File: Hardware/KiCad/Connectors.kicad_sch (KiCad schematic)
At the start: 55 parts

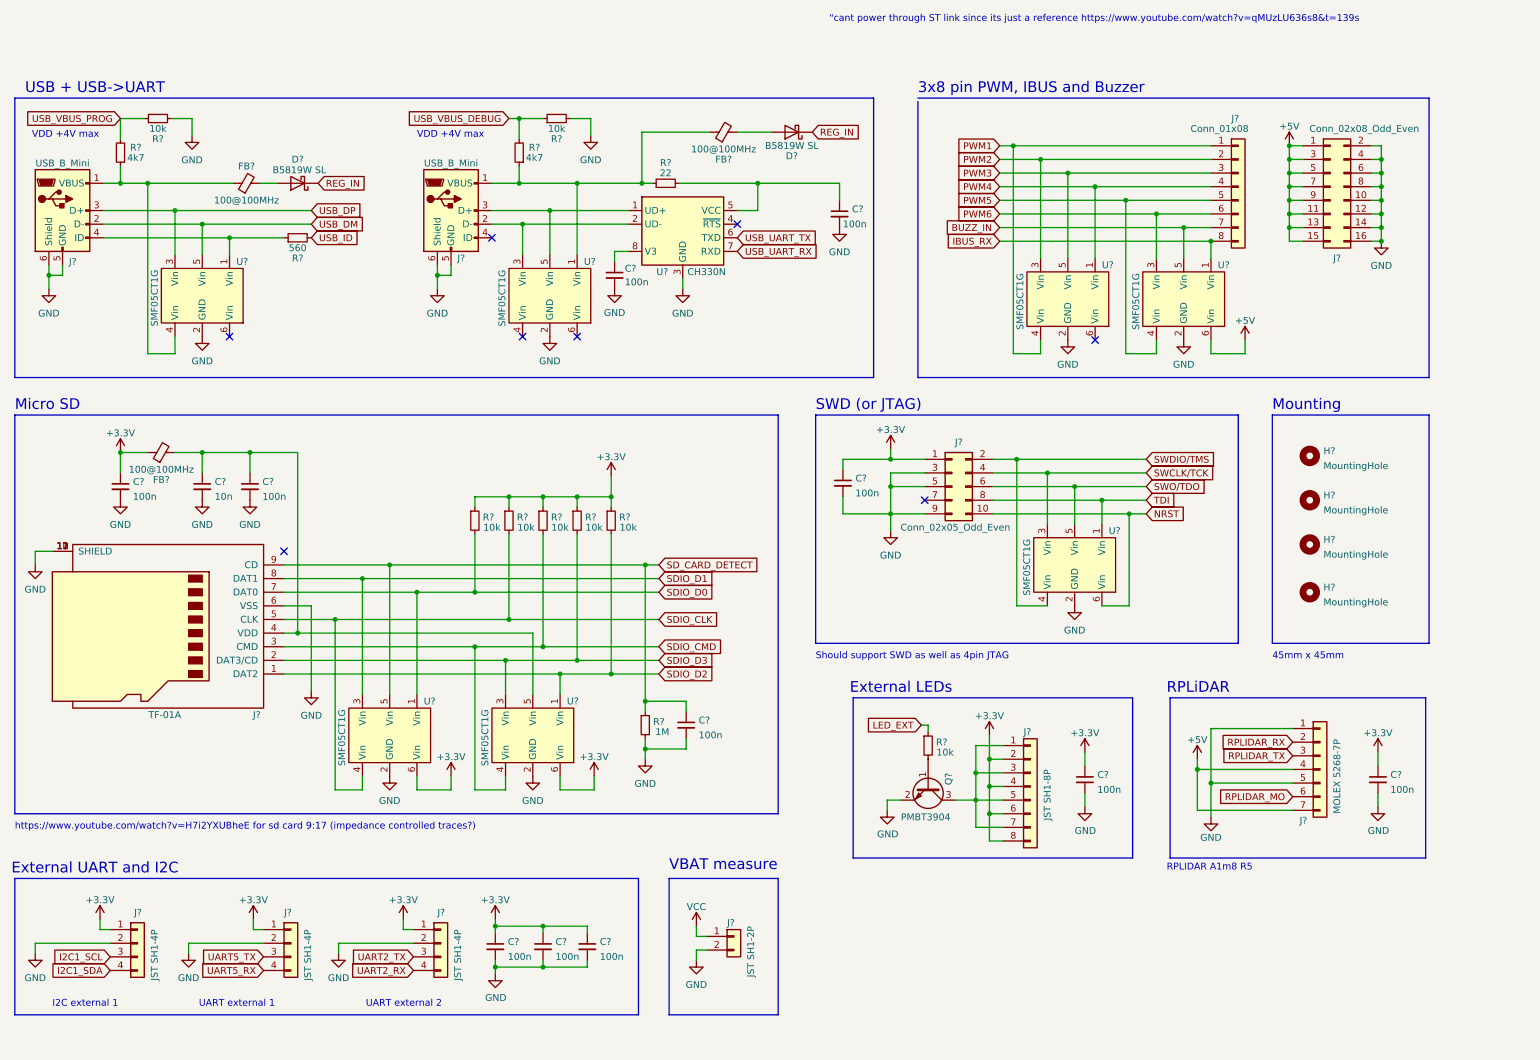
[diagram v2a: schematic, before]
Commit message: Fixed pullup connected to SDIO CLK
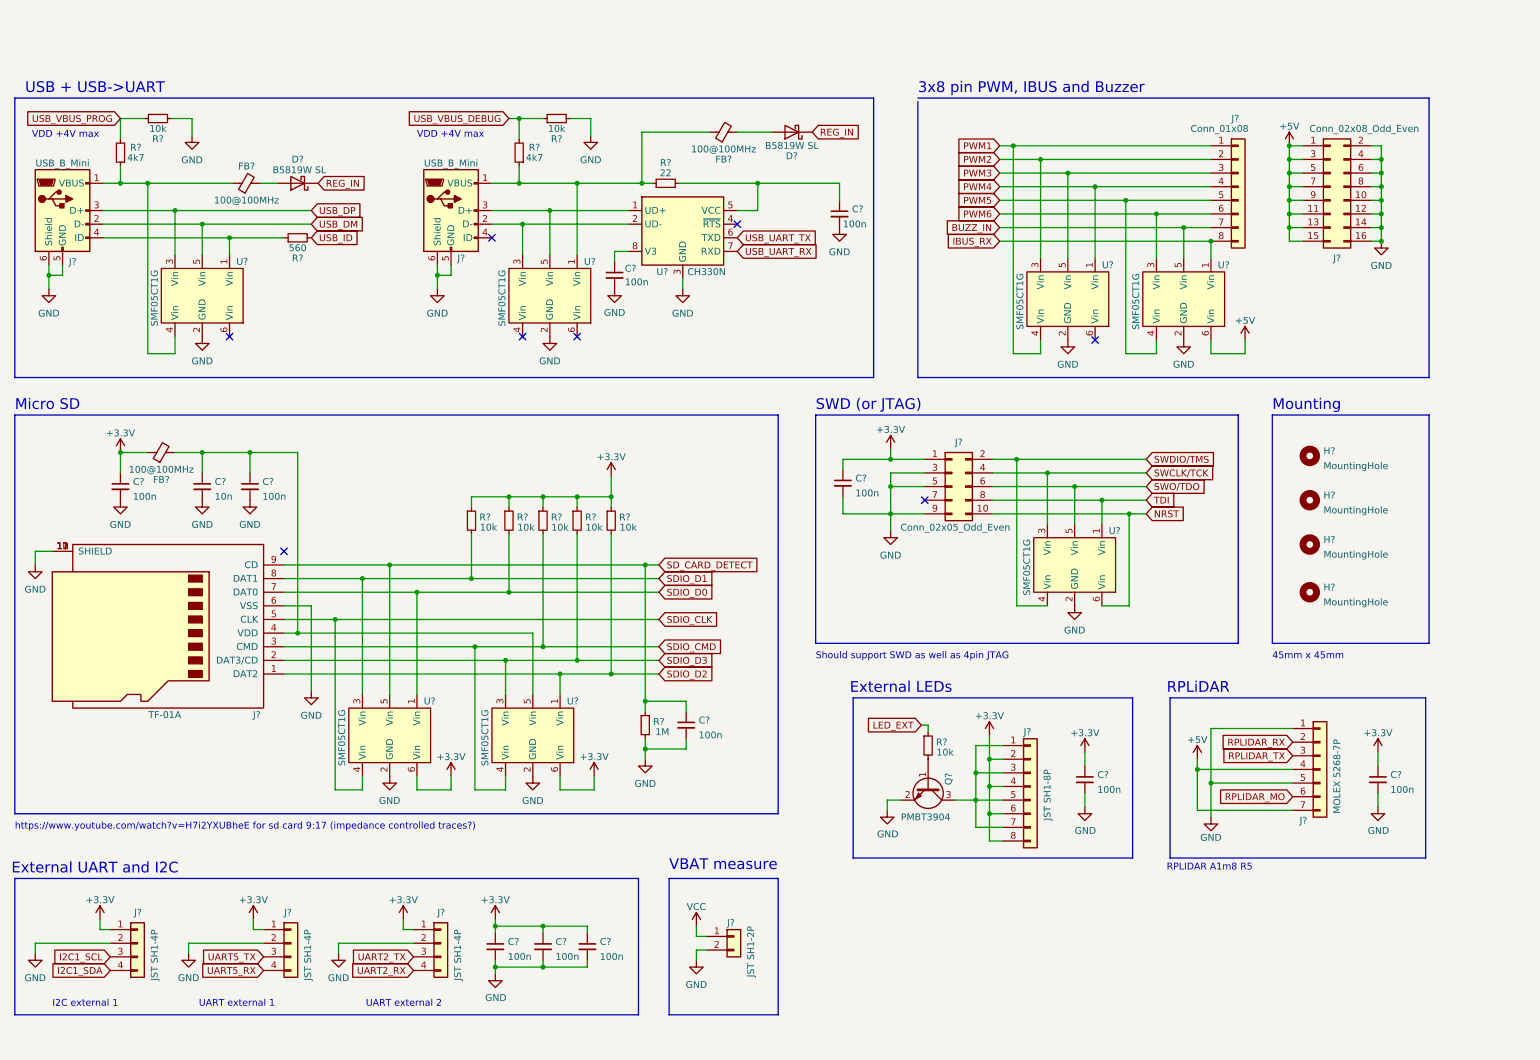
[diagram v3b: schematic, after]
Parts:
- removed R?: 10k, Resistor_SMD:R_0402_1005Metric, symbol Device:R_Small
- added R?: 10k, Resistor_SMD:R_0402_1005Metric, symbol Device:R_Small
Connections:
- net +3V3: now also R?.1
- net SDIO_D1: now also R?.2
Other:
- note removed: ""cant power through ST link since its just a reference https://www.youtube.com/watch?v=qMUzLU636s8&t=139s"
- moved on the sheet: R?
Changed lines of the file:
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@@
   (junction (at 232.41 43.18) (diameter 0) (color 0 0 0 0)
   )
+  (junction (at 116.205 126.365) (diameter 0) (color 0 0 0 0)
+  )
+  (junction (at 252.095 38.1) (diameter 0) (color 0 0 0 0)
+  )
+  (junction (at 196.215 147.32) (diameter 0) (color 0 0 0 0)
+  )
+  (junction (at 125.73 93.345) (diameter 0) (color 0 0 0 0)
+  )
+  (junction (at 227.33 40.64) (diameter 0) (color 0 0 0 0)
+  )
+  (junction (at 54.61 45.085) (diameter 0) (color 0 0 0 0)
+  )
   (junction (at 106.68 93.345) (diameter 0) (color 0 0 0 0)
   )
-  (junction (at 116.205 126.365) (diameter 0) (color 0 0 0 0)
-  )
-  (junction (at 252.095 38.1) (diameter 0) (color 0 0 0 0)
-  )
-  (junction (at 196.215 147.32) (diameter 0) (color 0 0 0 0)
-  )
-  (junction (at 125.73 93.345) (diameter 0) (color 0 0 0 0)
-  )
-  (junction (at 227.33 40.64) (diameter 0) (color 0 0 0 0)
-  )
-  (junction (at 54.61 45.085) (diameter 0) (color 0 0 0 0)
-  )
   (junction (at 108.585 34.925) (diameter 0) (color 0 0 0 0)
   )
@@
   (junction (at 217.17 93.98) (diameter 0) (color 0 0 0 0)
   )
-  (junction (at 106.68 116.205) (diameter 0) (color 0 0 0 0)
-  )
   (junction (at 196.215 142.24) (diameter 0) (color 0 0 0 0)
   )
@@
   (junction (at 269.24 33.02) (diameter 0) (color 0 0 0 0)
   )
+  (junction (at 106.68 111.125) (diameter 0) (color 0 0 0 0)
+  )
   (junction (at 132.08 106.045) (diameter 0) (color 0 0 0 0)
   )
+  (junction (at 99.695 108.585) (diameter 0) (color 0 0 0 0)
+  )
   (junction (at 34.29 34.925) (diameter 0) (color 0 0 0 0)
   )
@@
   )
   (junction (at 269.24 40.64) (diameter 0) (color 0 0 0 0)
-  )
-  (junction (at 100.33 111.125) (diameter 0) (color 0 0 0 0)
   )
   (junction (at 20.955 52.07) (diameter 0) (color 0 0 0 0)
@@
     (stroke (width 0) (type default) (color 0 0 0 0))
   )
-  (wire (pts (xy 74.295 116.205) (xy 106.68 116.205))
+  (wire (pts (xy 74.295 116.205) (xy 134.62 116.205))
     (stroke (width 0) (type default) (color 0 0 0 0))
   )
@@
     (stroke (width 0) (type default) (color 0 0 0 0))
   )
-  (wire (pts (xy 106.68 93.345) (xy 106.68 95.25))
-    (stroke (width 0) (type default) (color 0 0 0 0))
-  )
   (wire (pts (xy 131.445 25.4) (xy 131.445 34.925))
     (stroke (width 0) (type default) (color 0 0 0 0))
@@
     (stroke (width 0) (type default) (color 0 0 0 0))
   )
-  (wire (pts (xy 100.33 95.25) (xy 100.33 93.345))
+  (wire (pts (xy 106.68 95.25) (xy 106.68 93.345))
     (stroke (width 0) (type default) (color 0 0 0 0))
   )
@@
     (stroke (width 0) (type default) (color 0 0 0 0))
   )
+  (wire (pts (xy 106.68 93.345) (xy 113.03 93.345))
+    (stroke (width 0) (type default) (color 0 0 0 0))
+  )
   (wire (pts (xy 64.77 113.665) (xy 69.85 113.665))
     (stroke (width 0) (type default) (color 0 0 0 0))
@@
     (stroke (width 0) (type default) (color 0 0 0 0))
   )
-  (wire (pts (xy 79.375 108.585) (xy 134.62 108.585))
+  (wire (pts (xy 79.375 108.585) (xy 99.695 108.585))
     (stroke (width 0) (type default) (color 0 0 0 0))
   )
@@
     (stroke (width 0) (type default) (color 0 0 0 0))
   )
-  (wire (pts (xy 100.33 111.125) (xy 134.62 111.125))
-    (stroke (width 0) (type default) (color 0 0 0 0))
-  )
   (wire (pts (xy 31.115 40.005) (xy 44.45 40.005))
     (stroke (width 0) (type default) (color 0 0 0 0))
@@
     (stroke (width 0) (type default) (color 0 0 0 0))
   )
-  (wire (pts (xy 100.33 93.345) (xy 106.68 93.345))
+  (wire (pts (xy 99.695 93.345) (xy 106.68 93.345))
     (stroke (width 0) (type default) (color 0 0 0 0))
   )
@@
     (stroke (width 0) (type default) (color 0 0 0 0))
   )
+  (wire (pts (xy 99.695 95.25) (xy 99.695 93.345))
+    (stroke (width 0) (type default) (color 0 0 0 0))
+  )
   (wire (pts (xy 269.24 35.56) (xy 269.24 33.02))
     (stroke (width 0) (type default) (color 0 0 0 0))
@@
     (stroke (width 0) (type default) (color 0 0 0 0))
   )
-  (wire (pts (xy 89.535 111.125) (xy 100.33 111.125))
-    (stroke (width 0) (type default) (color 0 0 0 0))
-  )
   (wire (pts (xy 113.03 179.705) (xy 113.03 180.975))
     (stroke (width 0) (type default) (color 0 0 0 0))
@@
     (stroke (width 0) (type default) (color 0 0 0 0))
   )
-  (wire (pts (xy 106.68 116.205) (xy 134.62 116.205))
-    (stroke (width 0) (type default) (color 0 0 0 0))
-  )
   (wire (pts (xy 121.92 22.86) (xy 121.92 26.035))
     (stroke (width 0) (type default) (color 0 0 0 0))
@@
     (stroke (width 0) (type default) (color 0 0 0 0))
   )
-  (wire (pts (xy 100.33 100.33) (xy 100.33 111.125))
+  (wire (pts (xy 106.68 100.33) (xy 106.68 111.125))
     (stroke (width 0) (type default) (color 0 0 0 0))
   )
@@
     (stroke (width 0) (type default) (color 0 0 0 0))
   )
+  (wire (pts (xy 89.535 111.125) (xy 106.68 111.125))
+    (stroke (width 0) (type default) (color 0 0 0 0))
+  )
   (wire (pts (xy 64.77 108.585) (xy 79.375 108.585))
     (stroke (width 0) (type default) (color 0 0 0 0))
@@
     (stroke (width 0) (type default) (color 0 0 0 0))
   )
+  (wire (pts (xy 106.68 111.125) (xy 134.62 111.125))
+    (stroke (width 0) (type default) (color 0 0 0 0))
+  )
   (wire (pts (xy 74.93 176.53) (xy 88.9 176.53))
     (stroke (width 0) (type default) (color 0 0 0 0))
@@
     (stroke (width 0) (type default) (color 0 0 0 0))
   )
-  (wire (pts (xy 106.68 100.33) (xy 106.68 116.205))
-    (stroke (width 0) (type default) (color 0 0 0 0))
-  )
   (wire (pts (xy 106.045 147.955) (xy 100.33 147.955))
     (stroke (width 0) (type default) (color 0 0 0 0))
@@
     (stroke (width 0) (type default) (color 0 0 0 0))
   )
+  (wire (pts (xy 99.695 100.33) (xy 99.695 108.585))
+    (stroke (width 0) (type default) (color 0 0 0 0))
+  )
   (wire (pts (xy 205.74 30.48) (xy 205.74 48.895))
     (stroke (width 0) (type default) (color 0 0 0 0))
   )
+  (wire (pts (xy 99.695 108.585) (xy 134.62 108.585))
+    (stroke (width 0) (type default) (color 0 0 0 0))
+  )
   (polyline (pts (xy 174.625 19.05) (xy 14.605 19.05))
     (stroke (width 0) (type default) (color 0 0 0 0))
   )
   (wire (pts (xy 200.66 27.94) (xy 237.49 27.94))
-    (stroke (width 0) (type default) (color 0 0 0 0))
-  )
-  (wire (pts (xy 106.68 93.345) (xy 113.03 93.345))
     (stroke (width 0) (type default) (color 0 0 0 0))
   )
@@
   )
   (text "UART external 2" (at 80.01 188.595 0)
-    (effects (font (size 1.27 1.27)) (justify left bottom))
-  )
-  (text "\"cant power through ST link since its just a reference https://www.youtube.com/watch?v=qMUzLU636s8&t=139s"
-    (at 166.37 5.08 0)
     (effects (font (size 1.27 1.27)) (justify left bottom))
   )
@@
     (pin "1")
   )
-  (symbol (lib_id "Device:R_Small") (at 106.68 97.79 0) (unit 1)
-    (in_bom yes) (on_board yes)
-    (property "Reference" "R?" (id 0) (at 109.22 97.155 0))
-    (property "Value" "10k" (id 1) (at 109.855 99.06 0))
-    (property "Footprint" "Resistor_SMD:R_0402_1005Metric" (id 2) (at 106.68 97.79 0)
-      (effects (font (size 1.27 1.27)) hide)
-    )
-    (property "Datasheet" "~" (id 3) (at 106.68 97.79 0)
-      (effects (font (size 1.27 1.27)) hide)
-    )
-    (pin "1")
-    (pin "2")
-  )
   (symbol (lib_id "Device:C_Small") (at 113.03 177.165 0) (unit 1)
     (in_bom yes) (on_board yes) (fields_autoplaced)
@@
     (pin "5")
     (pin "6")
+  )
+  (symbol (lib_id "Device:R_Small") (at 99.695 97.79 0) (unit 1)
+    (in_bom yes) (on_board yes)
+    (property "Reference" "R?" (id 0) (at 102.235 97.155 0))
+    (property "Value" "10k" (id 1) (at 102.87 99.06 0))
+    (property "Footprint" "Resistor_SMD:R_0402_1005Metric" (id 2) (at 99.695 97.79 0)
+      (effects (font (size 1.27 1.27)) hide)
+    )
+    (property "Datasheet" "~" (id 3) (at 99.695 97.79 0)
+      (effects (font (size 1.27 1.27)) hide)
+    )
+    (pin "1")
+    (pin "2")
   )
   (symbol (lib_id "power:GND") (at 46.99 178.435 0) (unit 1)
@@
     (pin "1")
   )
-  (symbol (lib_id "Device:R_Small") (at 100.33 97.79 0) (unit 1)
-    (in_bom yes) (on_board yes)
-    (property "Reference" "R?" (id 0) (at 102.87 97.155 0))
-    (property "Value" "10k" (id 1) (at 103.505 99.06 0))
-    (property "Footprint" "Resistor_SMD:R_0402_1005Metric" (id 2) (at 100.33 97.79 0)
-      (effects (font (size 1.27 1.27)) hide)
-    )
-    (property "Datasheet" "~" (id 3) (at 100.33 97.79 0)
-      (effects (font (size 1.27 1.27)) hide)
-    )
+  (symbol (lib_id "Device:R_Small") (at 106.68 97.79 0) (unit 1)
+    (in_bom yes) (on_board yes)
+    (property "Reference" "R?" (id 0) (at 109.22 97.155 0))
+    (property "Value" "10k" (id 1) (at 109.855 99.06 0))
+    (property "Footprint" "Resistor_SMD:R_0402_1005Metric" (id 2) (at 106.68 97.79 0)
+      (effects (font (size 1.27 1.27)) hide)
+    )
+    (property "Datasheet" "~" (id 3) (at 106.68 97.79 0)
+      (effects (font (size 1.27 1.27)) hide)
+    )
